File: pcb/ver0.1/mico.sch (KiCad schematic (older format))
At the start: 41 parts, among them J1 USB_A, J2 SWD Prog, U1 MCP1702, U2 MP23DB01HPTR, U3 W25Q128JV, U4 RP2040, U5 logo, Y1 H130B-12.000-20-3050-EXT-TR

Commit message: 4 mic array schematic
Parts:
- added C? (x4): 1uF, Capacitor_SMD:C_0402_1005Metric, symbol Device:C_Small
- added C? (x4): 0.1uF, Capacitor_SMD:C_0402_1005Metric, symbol Device:C_Small
- added R? (x8): 10K, Resistor_SMD:R_0402_1005Metric, symbol Device:R_Small
- added U? (x4): MP23DB01HPTR, mico:MIC_SPH0641LU4H-1, symbol mico:MP23DB01HPTR
- J1: symbol Connector:USB_A -> mico-rescue:USB_A-Connector
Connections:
- net labels added: MIC_DOUT_0, MIC_DOUT_1, MIC_DOUT_2, MIC_DOUT_3
- wire segments 165 -> 236
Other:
- note added: "PDM Microphone Array"

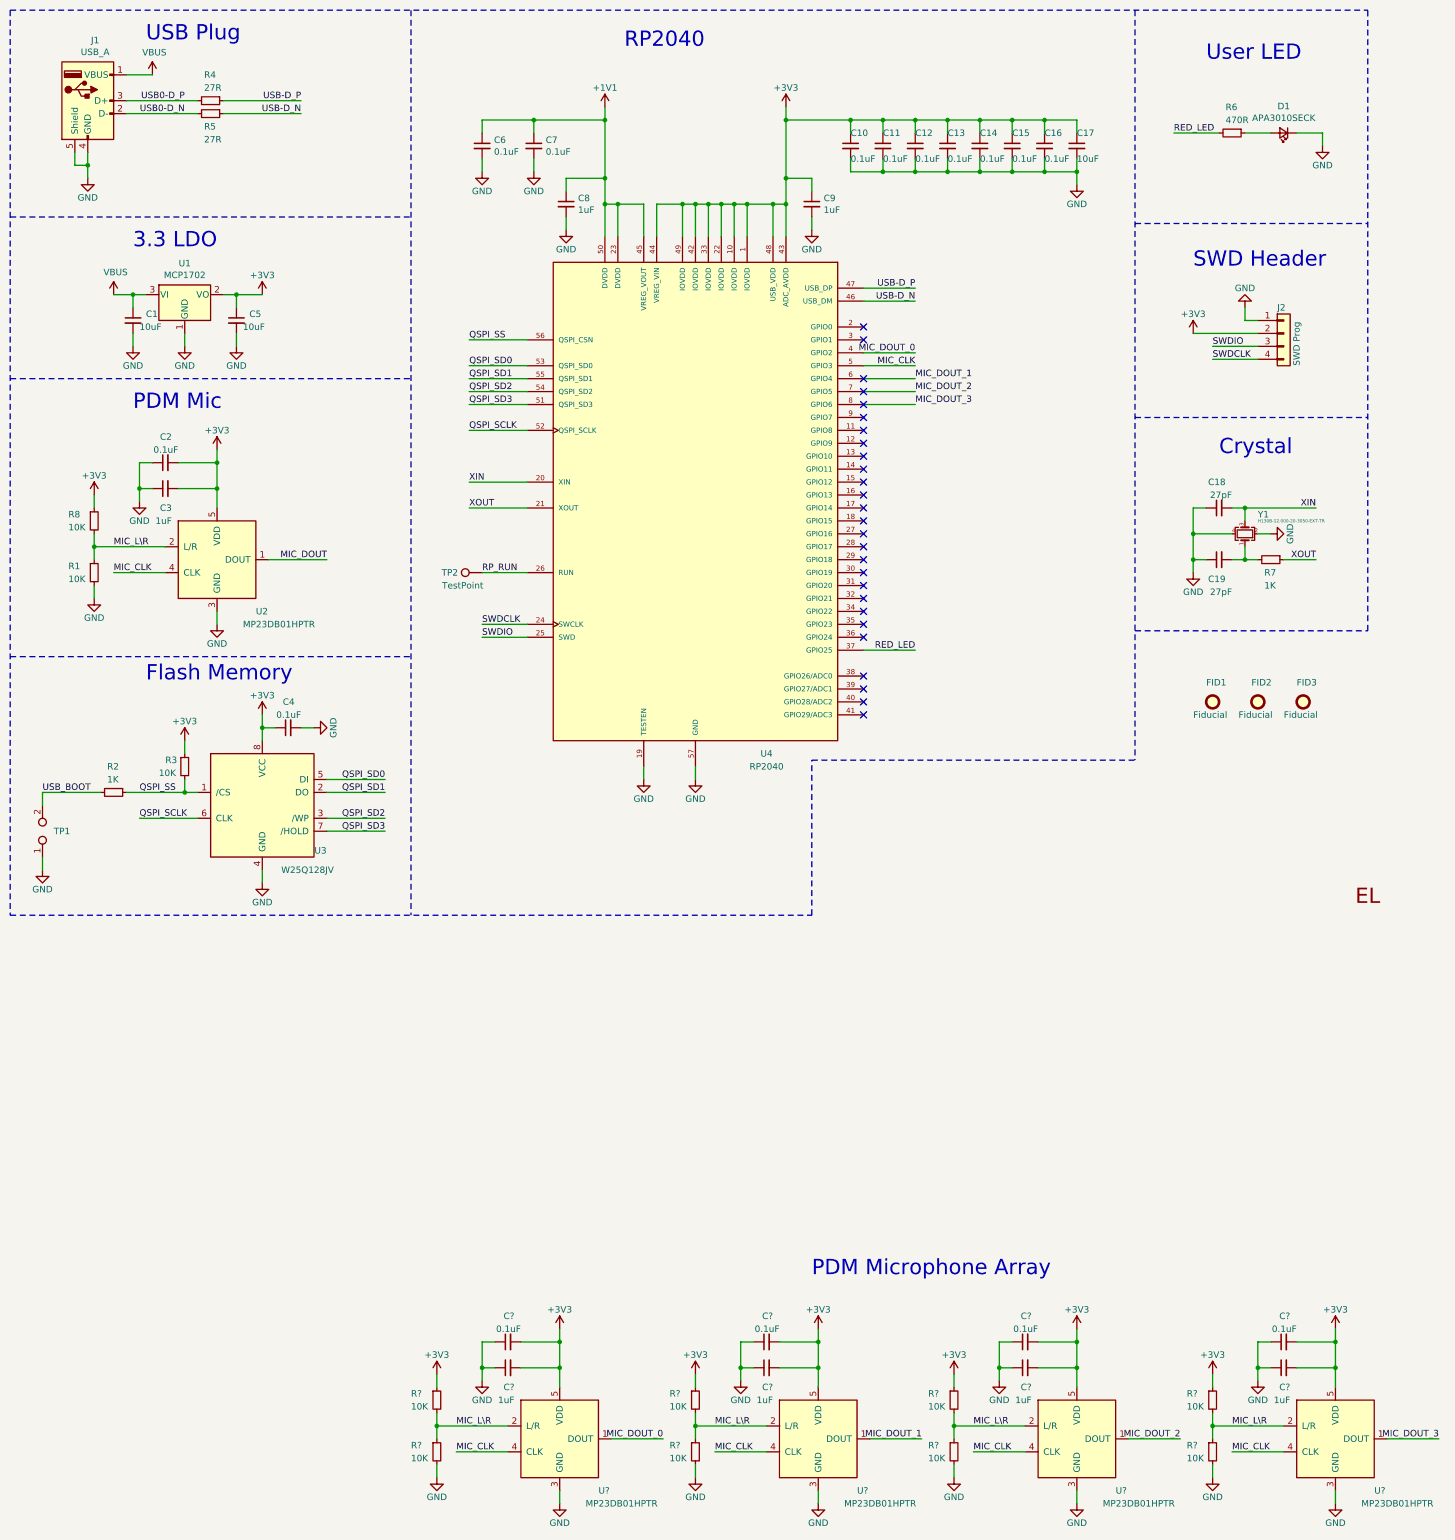
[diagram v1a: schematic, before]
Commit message: finsh schematic, resize pcb layers and edge cuts for 140mm mic array
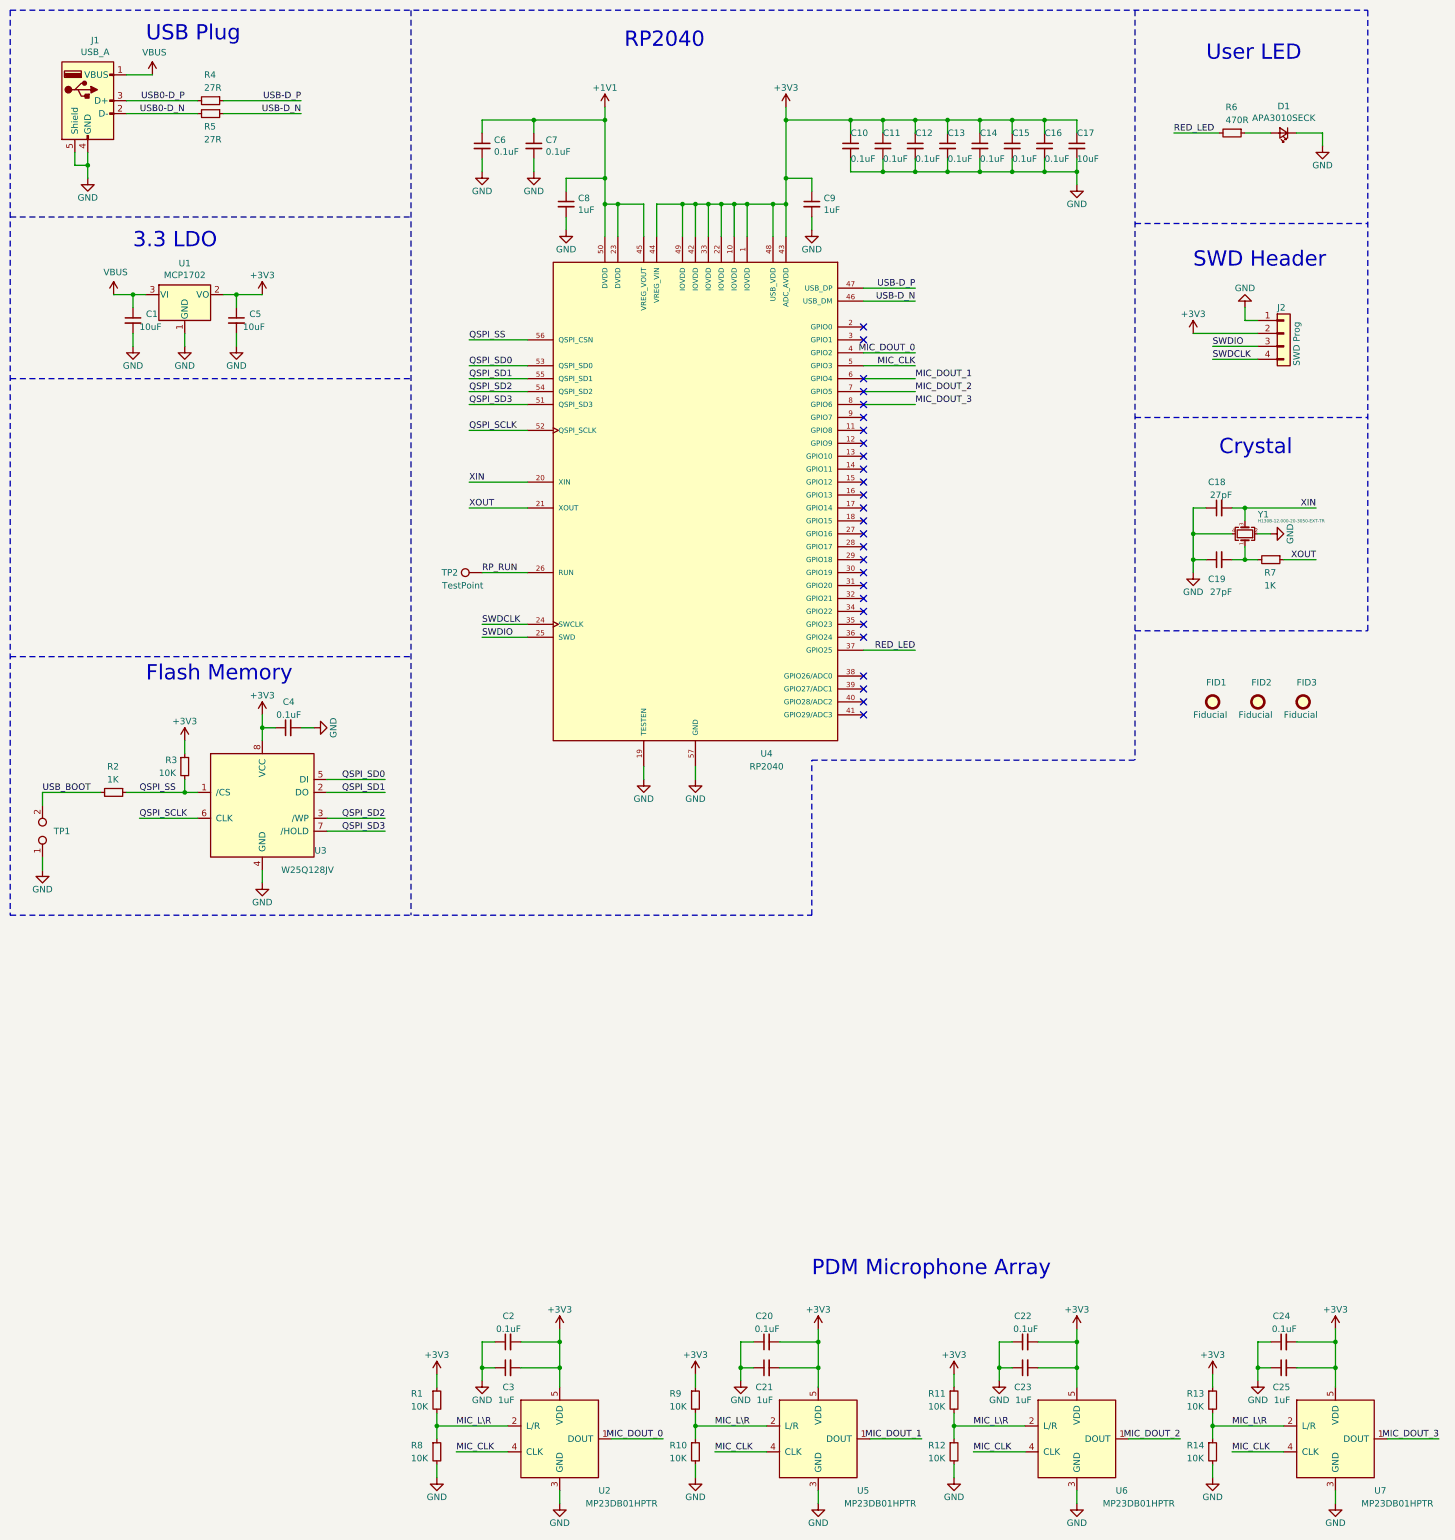
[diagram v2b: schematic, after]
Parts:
- removed C2: 0.1uF, Capacitor_SMD:C_0402_1005Metric, symbol Device:C_Small
- removed C3: 1uF, Capacitor_SMD:C_0402_1005Metric, symbol Device:C_Small
- removed R1, R8: 10K, Resistor_SMD:R_0402_1005Metric, symbol Device:R_Small
- removed U2: MP23DB01HPTR, mico:MIC_SPH0641LU4H-1, symbol mico:MP23DB01HPTR
- removed U5: logo, mico:el_logo-9P4_3P1, symbol mico:logo
- gave numbers to parts that had none: 20
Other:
- note removed: "PDM Mic"
